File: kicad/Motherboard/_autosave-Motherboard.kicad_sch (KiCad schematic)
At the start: 26 parts, among them J1 USB_C_Receptacle_USB2.0, Q1 DMN3404L, SW1 Reset, SW2 Boot, U1 CD74HC4067M, U2 CD74HC4067M, U3 TMC2208-LA, U4 LM2575-5.0BT, U5 CD74HC4067M, U6 CD74HC4067M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

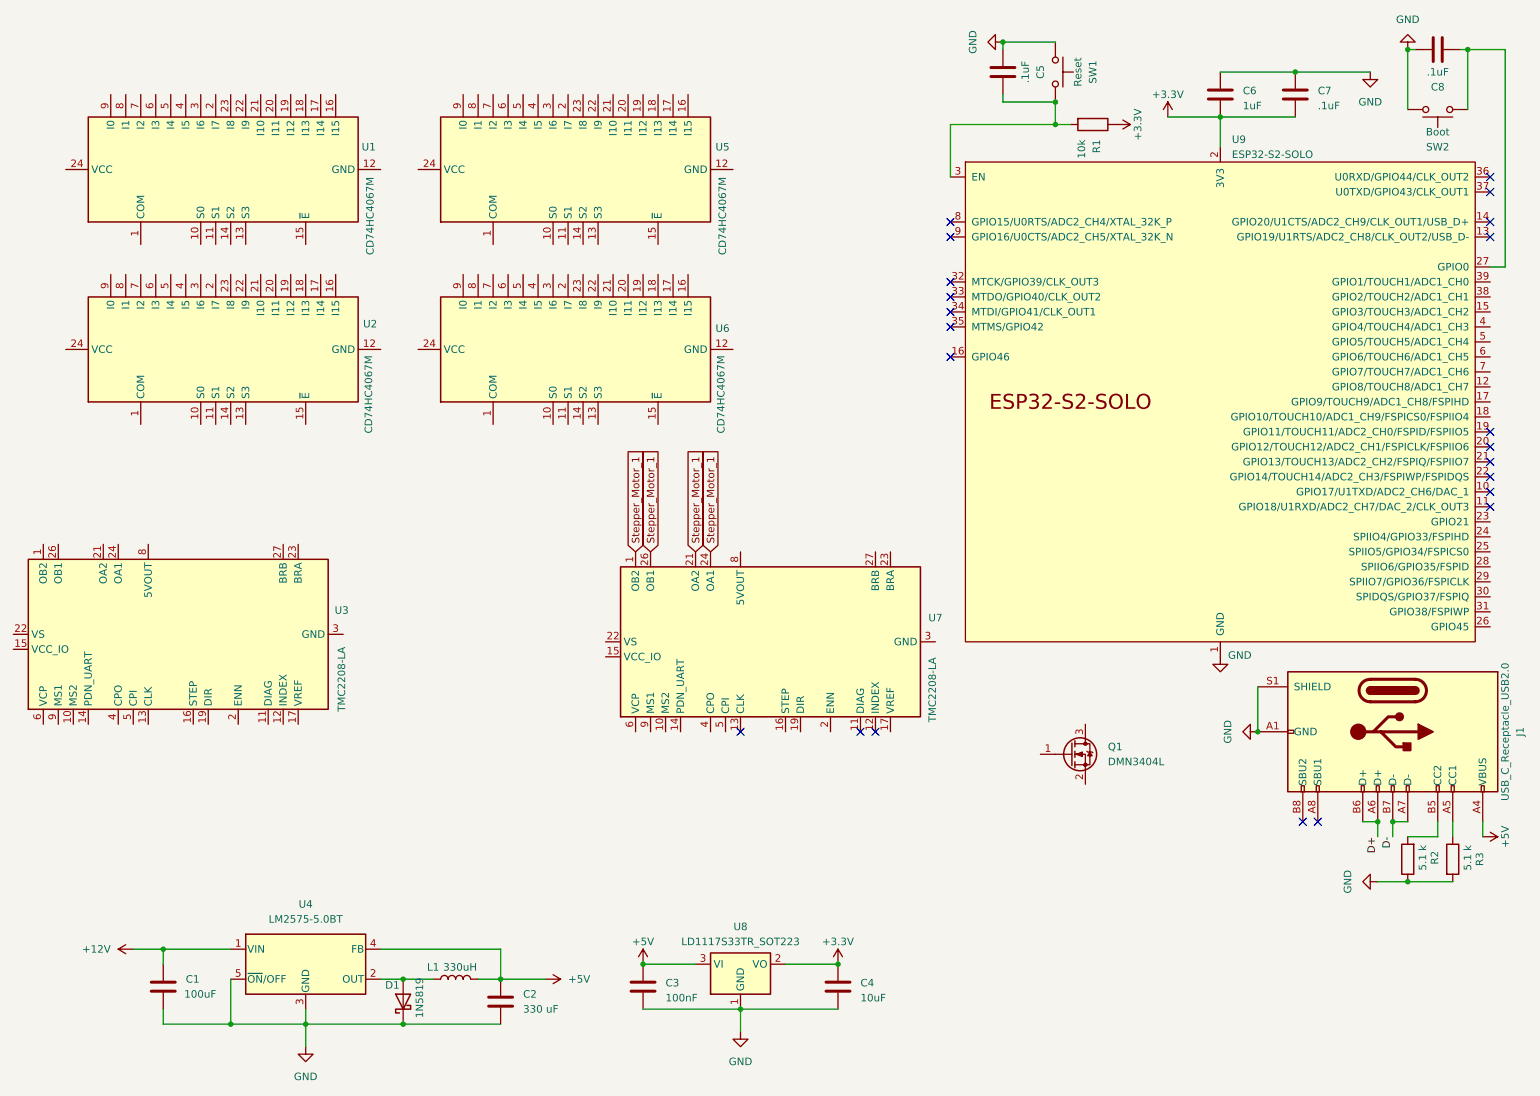
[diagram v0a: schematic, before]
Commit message: tcp2209 all passives done
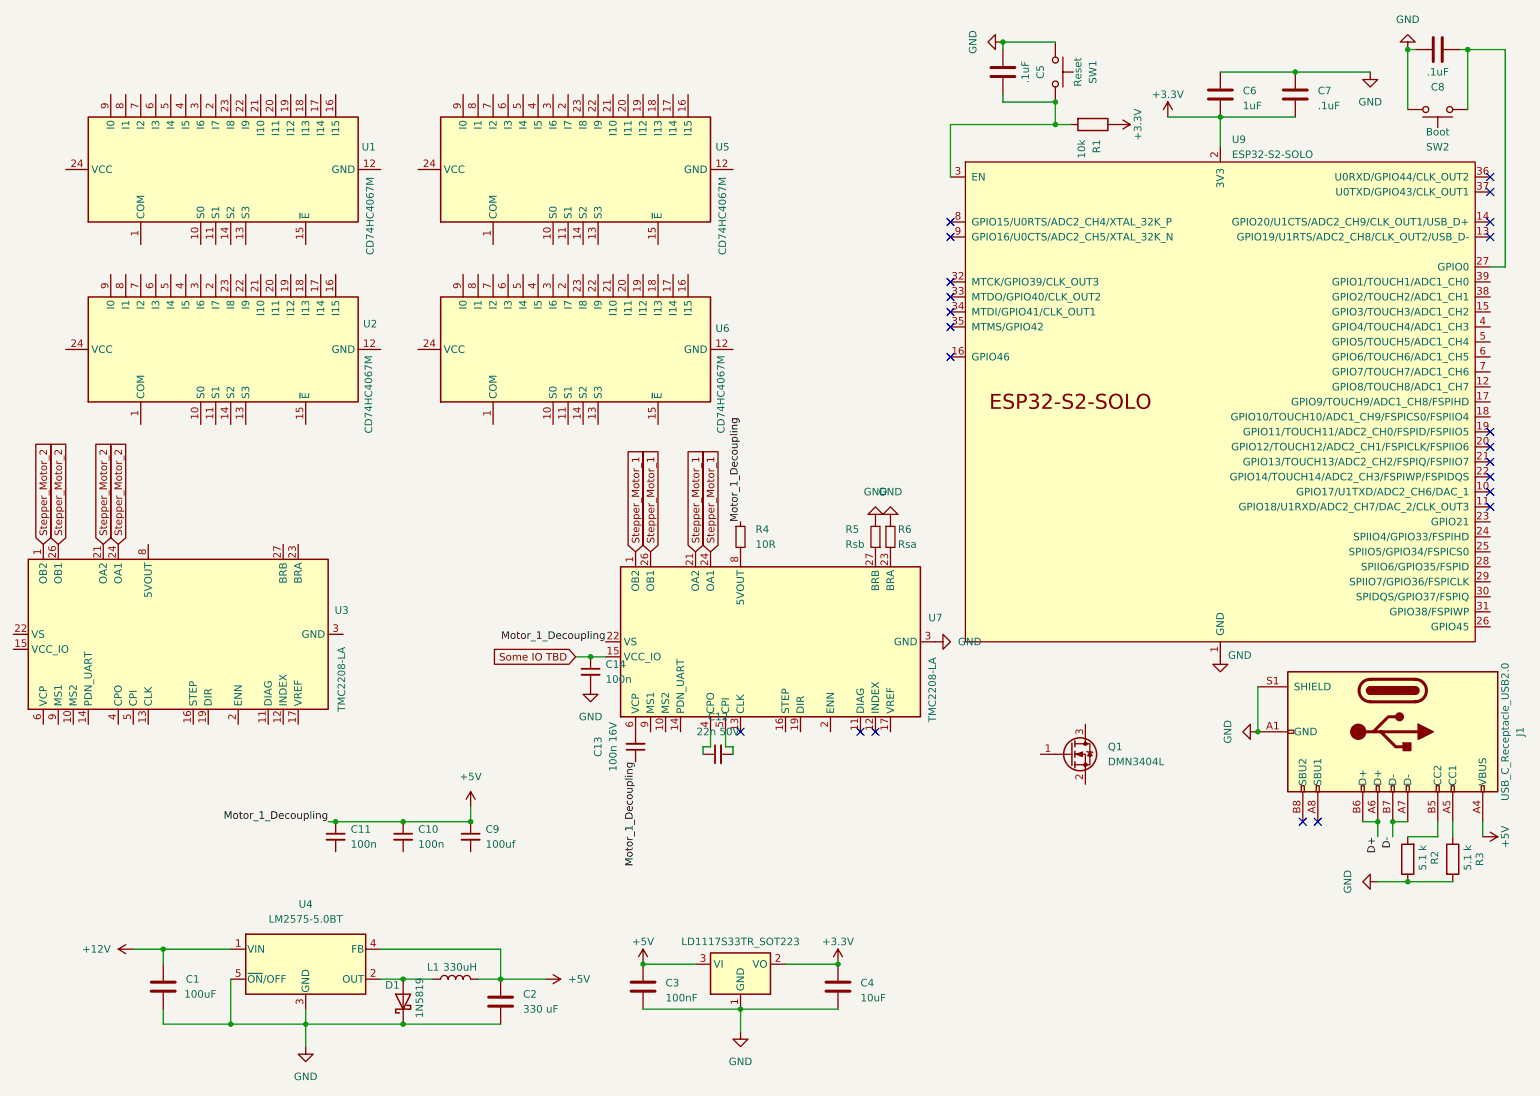
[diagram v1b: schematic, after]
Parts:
- added C10, C11, C14: 100n, symbol Device:C_Small
- added C12: 22n 50V, symbol Device:C_Small
- added C13: 100n 16V, symbol Device:C_Small
- added C9: 100uf, symbol Device:C_Small
- added R4: 10R, symbol Device:R_Small
- added R5: Rsb, symbol Device:R_Small
- added R6: Rsa, symbol Device:R_Small
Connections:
- net +5V: now also U7.22 (VS), U7.28 (VS), C10.1, C11.1, C13.1, C9.1, R4.1
- net GND: now also U7.18 (GND), U7.3 (GND), C14.2, R5.2, R6.1
- net Some IO TBD: now reaches U7.15 (VCC_IO)
- net Some IO TBD: now also C14.1
- net at U7.23 (BRA): now also R6.2
- net at U7.27 (BRB): now also R5.1
- net at U7.4 (CPO): now also C12.1
- net at U7.5 (CPI): now also C12.2
- net at U7.6 (VCP): now also C13.2
- net at U7.8 (5VOUT): now also R4.2
- net Stepper_Motor_2: now reaches U3.1 (OB2)
- net Stepper_Motor_2: now also U3.21 (OA2), U3.24 (OA1), U3.26 (OB1)
